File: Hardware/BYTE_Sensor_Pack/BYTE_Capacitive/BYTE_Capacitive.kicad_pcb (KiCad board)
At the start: 2 copper layers, 18 x 23 mm, 2 parts, among them J1 PCB

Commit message: update capacitive ICs
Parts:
- removed Ref**: Val**, BYTE_Sensors:Logo
- added C1: 100nF, Capacitor_SMD:C_0603_1608Metric, B.Cu at (154.1, 108.0)
- added C2: 0.1uF, Capacitor_SMD:C_0603_1608Metric, B.Cu at (152.2, 112.7)
- added C3: 1uF, Capacitor_SMD:C_0603_1608Metric, B.Cu at (151.6, 109.6)
- added C4: 1uF, Capacitor_SMD:C_0603_1608Metric, B.Cu at (158.6, 93.0)
- added C5: 1uF, Capacitor_SMD:C_0603_1608Metric, B.Cu at (153.7, 92.9)
- added R1: 2.2K, Resistor_SMD:R_0603_1608Metric, B.Cu at (144.6, 106.4)
- added R2: 2.2K, Resistor_SMD:R_0603_1608Metric, B.Cu at (143.1, 106.4)
- added R3: 2.2K, Resistor_SMD:R_0603_1608Metric, B.Cu at (146.1, 106.4)
- added U1: AD7147PACPZ-1500R7, BYTE_Sensors:QFN50P400X400X80-25N-D, B.Cu at (150.9, 105.5)
- added U2: DRV2605YZFR, BYTE_Sensors:BGA9C50P3X3_144X144X62, B.Cu at (156.1, 92.1)
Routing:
- net GND: track 0.00 -> 8.40 mm, vias 0 -> 2
- net /SDA: track 0.00 -> 7.99 mm
- net +3V3: track 0.00 -> 7.97 mm
- net /SCL: track 0.00 -> 7.33 mm
- net /INT: track 0.00 -> 3.21 mm
- net /ACSH: track 0.00 -> 2.77 mm
- net Net-(C1-Pad1): track 0.00 -> 2.55 mm
- net /REG: track 0.00 -> 2.09 mm
- net Net-(M1-Pad2): track 0.00 -> 1.24 mm
- net /EN: track 0.00 -> 1.23 mm
- net Net-(M1-Pad1): track 0.00 -> 1.23 mm
- net /IN_TRIG: track 0.00 -> 1.22 mm
- added copper zone on B.Cu, net GND
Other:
- net class BGA added: clearance 0.005, trace_width 0.075, via_dia 0.8, via_drill 0.4
- net class Default: clearance 0.2 -> 0.1; trace_width 0.25 -> 0.15
- rule trace_clearance: 0.2 -> 0.1
- rule trace_min: 0.2 -> 0.075

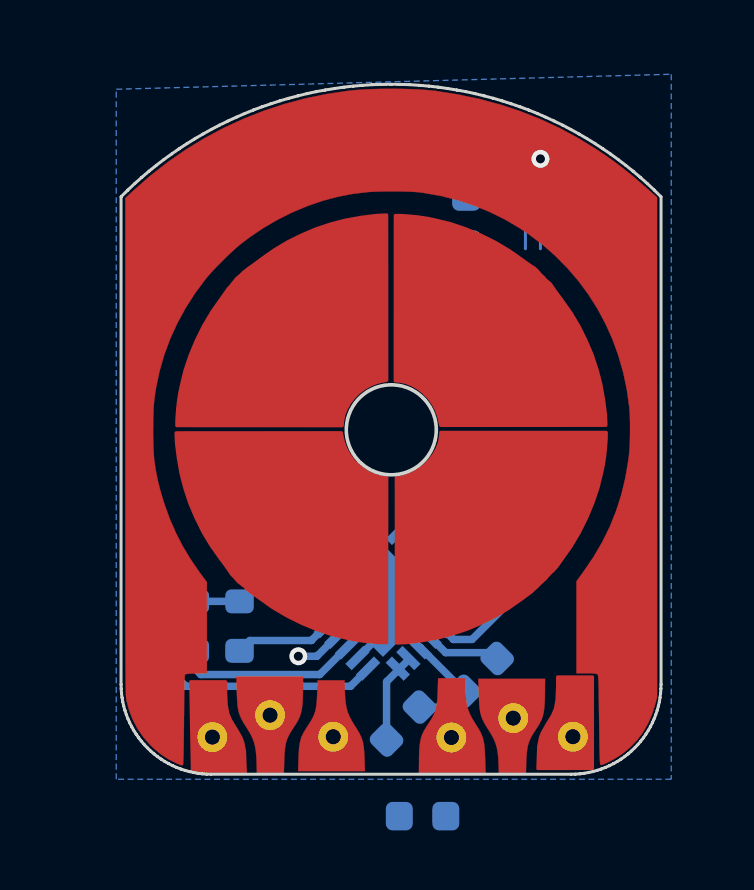
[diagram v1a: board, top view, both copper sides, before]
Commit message: update capacitive sensor board
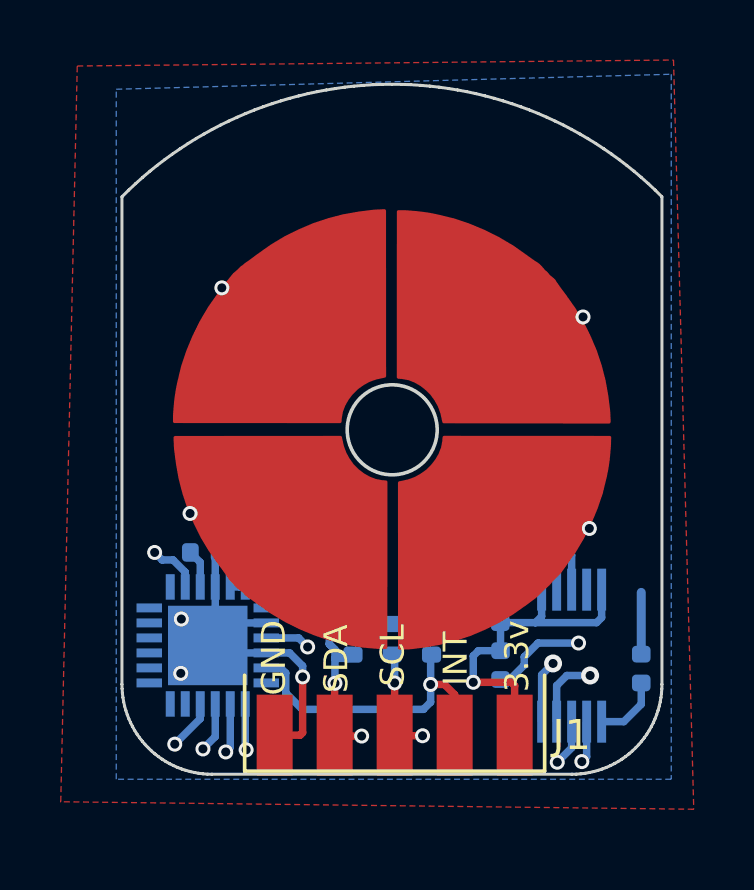
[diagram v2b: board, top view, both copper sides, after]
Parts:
- added Ref**: Val**, BYTE_Sensors:Logo, F.Cu at (146.6, 80.6)
- added T1: PCB, BYTE_Sensors:Capacitive_PCB_NoConnector, F.Cu at (152.1, 103.1)
- C1, C2, C3, C4, C5: footprint Capacitor_SMD:C_0603_1608Metric -> Capacitor_SMD:C_0402_1005Metric
- J1: value PCB -> input; footprint BYTE_Sensors:Capacitive_PCB -> BYTE_Sensors:Flex_Connector
- R1, R2, R3: footprint Resistor_SMD:R_0603_1608Metric -> Resistor_SMD:R_0402_1005Metric
- U2: value DRV2605YZFR -> DRV2605LDGST; footprint BYTE_Sensors:BGA9C50P3X3_144X144X62 -> BYTE_Sensors:SOP50P490X110-10N
- moved U2 15.3 mm to (157.2, 107.4)
- moved C4 14.8 mm to (159.5, 107.8), turned to 90 degrees
- moved C5 13.0 mm to (154.8, 105.8), turned to 90 degrees
- moved C1 10.1 mm to (144.9, 103.9), turned to 0 degrees
- moved C3 7.45 mm to (146.8, 103.9), turned to 180 degrees
- moved J1 6.99 mm to (151.3, 110.0)
- moved R2 6.76 mm to (149.9, 106.8)
- moved R1 6.59 mm to (151.2, 106.8)
- moved R3 6.42 mm to (152.5, 106.8)
- moved U1 6.03 mm to (145.1, 107.0), turned to 0 degrees
- moved C2 5.67 mm to (154.8, 107.7), turned to 270 degrees
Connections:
- J1 pad 1: Net-(J1-Pad1) -> GND
- J1 pad 2: Net-(J1-Pad2) -> /SDA
- J1 pad 3: Net-(J1-Pad3) -> /SCL
- J1 pad 4: Net-(J1-Pad4) -> /INT
- J1 pad 5: Net-(J1-Pad5) -> +3V3
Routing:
- net /CIN0: track 0.00 -> 33.9 mm, vias 0 -> 2
- net /CIN1: track 0.00 -> 28.0 mm, vias 0 -> 2
- net /CIN3: track 0.00 -> 24.6 mm, vias 0 -> 2
- net GND: track 8.40 -> 26.4 mm, vias 2 -> 4
- net +3V3: track 7.97 -> 24.4 mm, vias 0 -> 1
- net /CIN2: track 0.00 -> 14.6 mm, vias 0 -> 2
- net /SDA: track 7.99 -> 17.2 mm, vias 0 -> 3
- net /SCL: track 7.33 -> 16.0 mm, vias 0 -> 4
- net /INT: track 3.21 -> 10.4 mm, vias 0 -> 1
- net Net-(C1-Pad1): track 2.55 -> 1.29 mm
- net Net-(M1-Pad2): track 1.24 -> 0.00 mm
- net /IN_TRIG: track 1.22 -> 2.46 mm, vias 0 -> 1
- net Net-(M1-Pad1): track 1.23 -> 0.00 mm
- net /ACSH: track 2.77 -> 1.79 mm, vias 0 -> 1
- net /EN: track 1.23 -> 2.10 mm, vias 0 -> 1
- added copper zone on F.Cu, net /ACSH
- added copper zone on In1.Cu, net GND
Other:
- copper layers 2 -> 4
- board text added: "3.3v"
- board text added: "GND"
- board text added: "INT"
- board text added: "SCL"
- board text added: "SDA"

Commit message: modify magnetic
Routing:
- added copper zone on In2.Cu, net GND

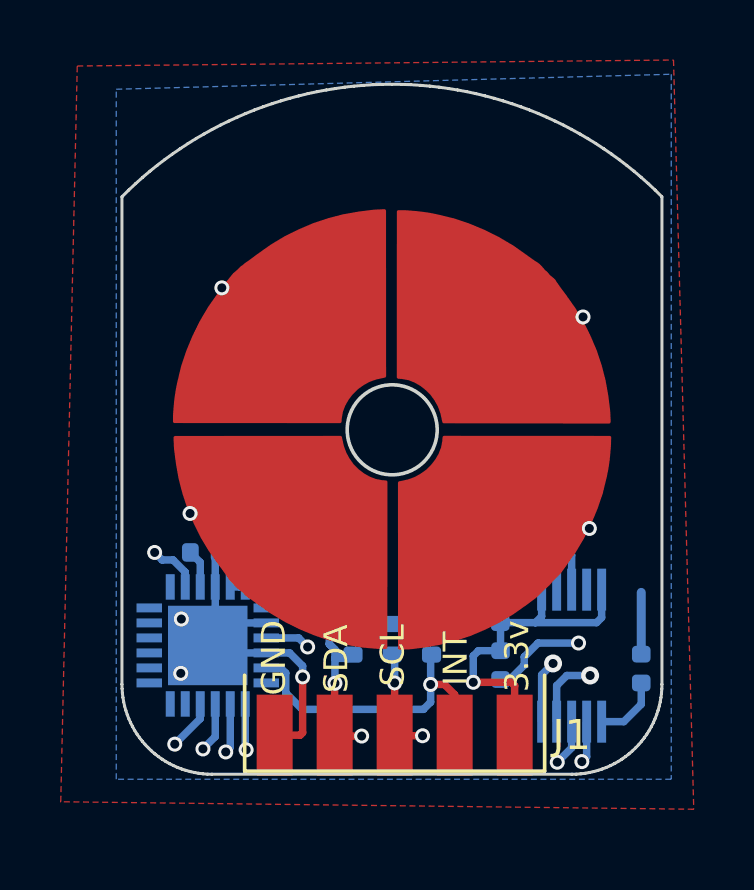
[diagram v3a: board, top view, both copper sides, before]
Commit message: add motor footprint
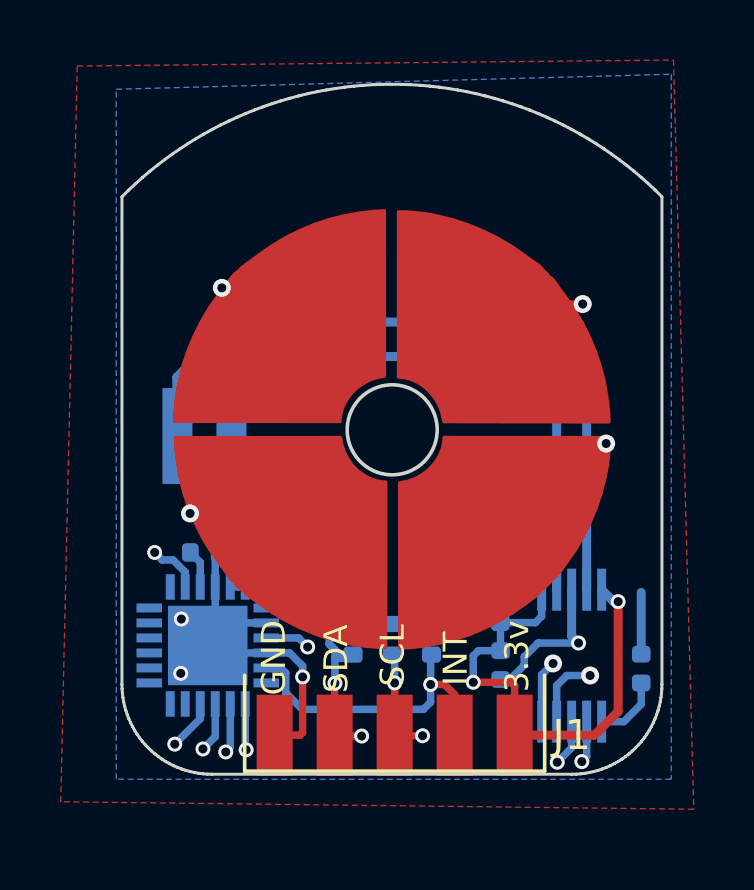
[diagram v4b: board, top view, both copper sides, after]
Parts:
- added M1: Motor_DC, BYTE_Sensors:VLV041235L, B.Cu at (145.9, 100.7)
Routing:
- net Net-(M1-Pad1): track 0.00 -> 24.2 mm
- net Net-(M1-Pad2): track 0.00 -> 19.8 mm
- net +3V3: track 24.4 -> 29.3 mm, vias 1 -> 2
- net /CIN1: track 28.0 -> 31.9 mm
- net GND: track 26.4 -> 25.9 mm
